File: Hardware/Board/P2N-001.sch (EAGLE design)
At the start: 40 parts, among them IC1 4053N, IC2 LTC485N, IC3 74LS07N, IC4 LTC485N, K1 G5V1, T1 2SC1815, X1 HIROSE-DX10LM1-14SE

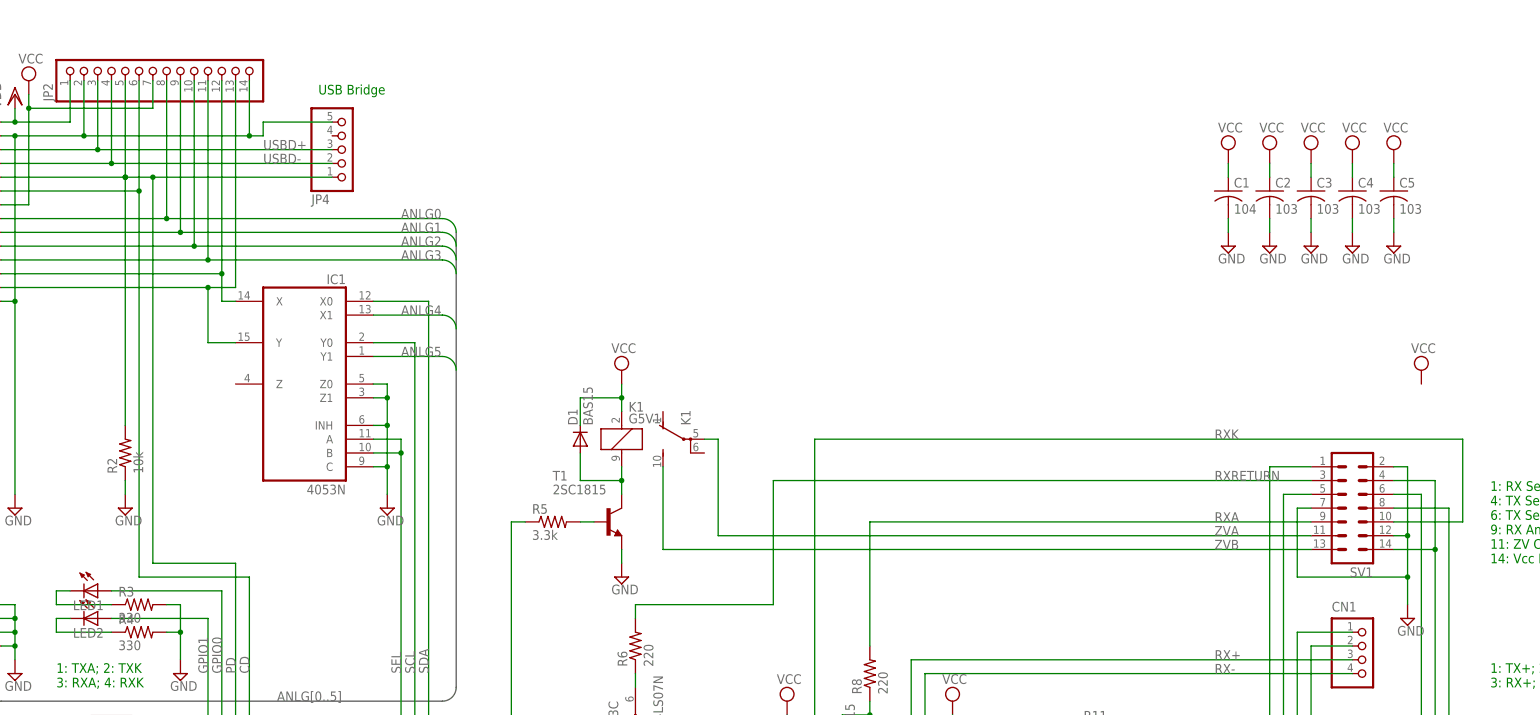
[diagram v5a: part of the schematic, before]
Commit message: Changed USB connector from Pinheader to Micro-B.
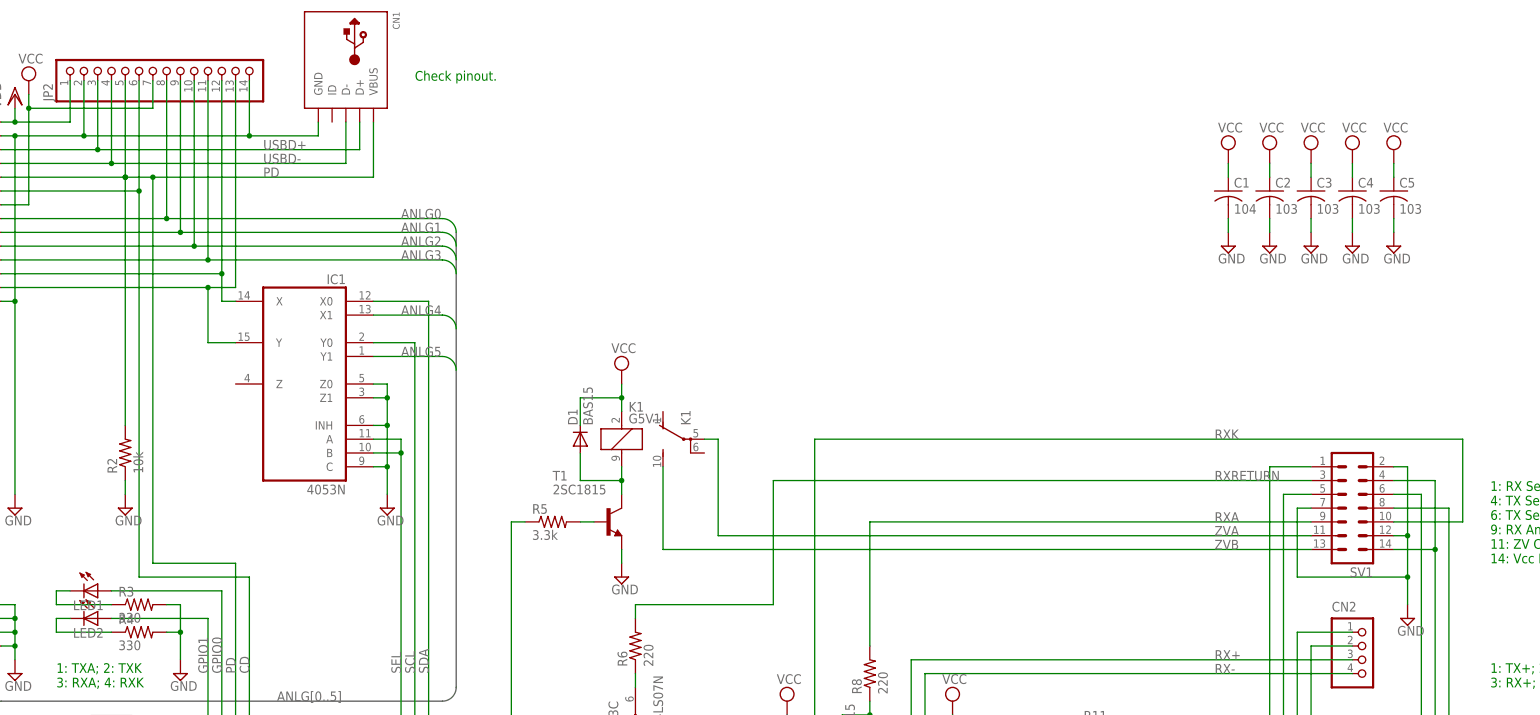
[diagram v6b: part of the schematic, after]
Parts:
- removed JP4: (no value), pinhead:PINHD-1X5/90
- added CN2: (no value), jst-ph:S4B-PH-K-S
- CN1: device jst-ph:S4B-PH-K-S -> adafruit:USBMINIB
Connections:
- net GND: now also CN1.GND; no longer JP4.5
- net PD: now also CN1.VBUS; no longer JP4.1
- net RX+: now also CN2.3; no longer CN1.3
- net RX-: now also CN2.4; no longer CN1.4
- net TX+: now also CN2.1; no longer CN1.1
- net TX-: now also CN2.2; no longer CN1.2
- net USBD+: now also CN1.D+; no longer JP4.3
- net USBD-: now also CN1.D-; no longer JP4.2
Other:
- note added: "Check pinout."
- note removed: "USB Bridge"
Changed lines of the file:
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@@
 <part name="SUPPLY26" library="supply2" deviceset="GND" device=""/>
 <part name="SUPPLY25" library="supply2" deviceset="VCC" device=""/>
-<part name="SUPPLY29" library="supply2" deviceset="GND" device=""/>
+<part name="SUPPLY28" library="supply2" deviceset="GND" device=""/>
 <part name="SUPPLY1" library="supply2" deviceset="VCC" device=""/>
 <part name="SUPPLY4" library="supply2" deviceset="VCC" device=""/>
@@
 <part name="R1" library="resistor" deviceset="R-US_" device="0204/5" value="150"/>
 <part name="SV1" library="con-ml" deviceset="ML14L" device=""/>
-<part name="JP4" library="pinhead" deviceset="PINHD-1X5" device="/90"/>
 <part name="R2" library="resistor" deviceset="R-US_" device="0204/5" value="10k"/>
 <part name="SUPPLY5" library="supply2" deviceset="GND" device=""/>
@@
 <part name="SUPPLY3" library="supply2" deviceset="GND" device=""/>
 <part name="JP1" library="pinhead" deviceset="PINHD-2X4" device=""/>
-<part name="SUPPLY28" library="supply2" deviceset="VCC" device=""/>
 <part name="K1" library="relay" deviceset="G5V1" device=""/>
-<part name="CN1" library="jst-ph" deviceset="S4B-PH-*" device="K-S"/>
+<part name="CN2" library="jst-ph" deviceset="S4B-PH-*" device="K-S"/>
 <part name="R3" library="resistor" deviceset="R-US_" device="0204/5" value="330"/>
 <part name="R4" library="resistor" deviceset="R-US_" device="0204/5" value="330"/>
@@
 <part name="R9" library="resistor" deviceset="R-US_" device="0204/5" value="220"/>
 <part name="R13" library="resistor" deviceset="R-US_" device="0204/5" value="220"/>
+<part name="CN1" library="adafruit" deviceset="USB" device="MINIB"/>
 </parts>
 <sheets>
@@
 7: LEDA; 8: LEDK</text>
 <text x="25.4" y="152.4" size="1.778" layer="91" rot="R90">GeekPort II</text>
-<text x="96.52" y="190.5" size="1.778" layer="91">USB Bridge</text>
 <text x="48.26" y="81.28" size="1.778" layer="91">1: TXA; 2: TXK
 3: RXA; 4: RXK</text>
@@
 11: ZV Contact A; 12: GND; 13: ZV Contact B;
 14: Vcc R220</text>
+<text x="114.3" y="193.04" size="1.778" layer="91">Check pinout.</text>
 </plain>
 <instances>
@@
 <instance part="IC3" gate="E" x="320.04" y="33.02"/>
 <instance part="IC3" gate="F" x="320.04" y="20.32"/>
-<instance part="SUPPLY29" gate="GND" x="307.34" y="10.16"/>
+<instance part="SUPPLY28" gate="GND" x="307.34" y="10.16"/>
 <instance part="SUPPLY1" gate="G$1" x="7.62" y="48.26"/>
 <instance part="SUPPLY4" gate="G$1" x="43.18" y="193.04"/>
@@
 <instance part="R1" gate="G$1" x="33.02" y="88.9"/>
 <instance part="SV1" gate="1" x="287.02" y="114.3" rot="R180"/>
-<instance part="JP4" gate="A" x="101.6" y="180.34" rot="MR180"/>
 <instance part="R2" gate="G$1" x="60.96" y="124.46" rot="R90"/>
 <instance part="SUPPLY5" gate="GND" x="60.96" y="114.3"/>
@@
 <instance part="SUPPLY3" gate="GND" x="40.64" y="83.82"/>
 <instance part="JP1" gate="A" x="17.78" y="91.44"/>
-<instance part="SUPPLY28" gate="G$1" x="299.72" y="139.7"/>
 <instance part="K1" gate="1" x="152.4" y="127"/>
 <instance part="K1" gate="2" x="165.1" y="127" rot="R90"/>
-<instance part="CN1" gate="G$1" x="287.02" y="88.9"/>
+<instance part="CN2" gate="G$1" x="287.02" y="88.9"/>
 <instance part="R3" gate="G$1" x="63.5" y="96.52"/>
 <instance part="R4" gate="G$1" x="63.5" y="91.44"/>
@@
 <instance part="R9" gate="G$1" x="220.98" y="68.58"/>
 <instance part="R13" gate="G$1" x="248.92" y="48.26"/>
+<instance part="CN1" gate="G$1" x="101.6" y="195.58" rot="R270"/>
 </instances>
 <busses>
@@
 </segment>
 <segment>
-<pinref part="SUPPLY29" gate="GND" pin="GND"/>
+<pinref part="SUPPLY28" gate="GND" pin="GND"/>
 <pinref part="IC3" gate="F" pin="I"/>
 <wire x1="307.34" y1="45.72" x2="307.34" y2="33.02" width="0.1524" layer="91"/>
@@
 <wire x1="40.64" y1="182.88" x2="53.34" y2="182.88" width="0.1524" layer="91"/>
 <wire x1="53.34" y1="182.88" x2="83.82" y2="182.88" width="0.1524" layer="91"/>
-<wire x1="83.82" y1="182.88" x2="86.36" y2="182.88" width="0.1524" layer="91"/>
-<wire x1="86.36" y1="182.88" x2="86.36" y2="185.42" width="0.1524" layer="91"/>
-<pinref part="JP4" gate="A" pin="5"/>
-<wire x1="86.36" y1="185.42" x2="99.06" y2="185.42" width="0.1524" layer="91"/>
 <junction x="40.64" y="182.88"/>
 <pinref part="JP2" gate="A" pin="2"/>
@@
 <pinref part="X1" gate="G$1" pin="-2"/>
 <pinref part="X1" gate="G$1" pin="-14"/>
+<pinref part="CN1" gate="G$1" pin="GND"/>
+<wire x1="83.82" y1="182.88" x2="96.52" y2="182.88" width="0.1524" layer="91"/>
+<wire x1="96.52" y1="182.88" x2="96.52" y2="185.42" width="0.1524" layer="91"/>
 </segment>
 <segment>
@@
 <wire x1="254" y1="30.48" x2="276.86" y2="30.48" width="0.1524" layer="91"/>
 <wire x1="276.86" y1="30.48" x2="276.86" y2="27.94" width="0.1524" layer="91"/>
-<pinref part="CN1" gate="G$1" pin="1"/>
+<pinref part="CN2" gate="G$1" pin="1"/>
 <wire x1="287.02" y1="91.44" x2="276.86" y2="91.44" width="0.1524" layer="91"/>
 <wire x1="276.86" y1="91.44" x2="276.86" y2="30.48" width="0.1524" layer="91"/>
@@
 <pinref part="IC2" gate="G$1" pin="A"/>
 <wire x1="175.26" y1="35.56" x2="205.74" y2="35.56" width="0.1524" layer="91"/>
-<pinref part="CN1" gate="G$1" pin="3"/>
+<pinref part="CN2" gate="G$1" pin="3"/>
 <wire x1="287.02" y1="86.36" x2="205.74" y2="86.36" width="0.1524" layer="91"/>
 <wire x1="205.74" y1="86.36" x2="205.74" y2="35.56" width="0.1524" layer="91"/>
@@
 <pinref part="IC2" gate="G$1" pin="B"/>
 <wire x1="182.88" y1="33.02" x2="180.34" y2="33.02" width="0.1524" layer="91"/>
-<pinref part="CN1" gate="G$1" pin="4"/>
+<pinref part="CN2" gate="G$1" pin="4"/>
 <wire x1="180.34" y1="33.02" x2="175.26" y2="33.02" width="0.1524" layer="91"/>
 <wire x1="287.02" y1="83.82" x2="208.28" y2="83.82" width="0.1524" layer="91"/>
@@
 <pinref part="R14" gate="G$1" pin="1"/>
 <wire x1="254" y1="27.94" x2="261.62" y2="27.94" width="0.1524" layer="91"/>
-<pinref part="CN1" gate="G$1" pin="2"/>
+<pinref part="CN2" gate="G$1" pin="2"/>
 <wire x1="261.62" y1="27.94" x2="264.16" y2="27.94" width="0.1524" layer="91"/>
 <wire x1="287.02" y1="88.9" x2="279.4" y2="88.9" width="0.1524" layer="91"/>
@@
 <net name="PD" class="0">
 <segment>
-<pinref part="JP4" gate="A" pin="1"/>
 <wire x1="38.1" y1="175.26" x2="60.96" y2="175.26" width="0.1524" layer="91"/>
 <wire x1="60.96" y1="175.26" x2="66.04" y2="175.26" width="0.1524" layer="91"/>
 <pinref part="R2" gate="G$1" pin="2"/>
 <junction x="60.96" y="175.26"/>
-<wire x1="66.04" y1="175.26" x2="99.06" y2="175.26" width="0.1524" layer="91"/>
+<wire x1="66.04" y1="175.26" x2="106.68" y2="175.26" width="0.1524" layer="91"/>
 <wire x1="60.96" y1="175.26" x2="60.96" y2="129.54" width="0.1524" layer="91"/>
 <pinref part="JP2" gate="A" pin="5"/>
@@
 <junction x="66.04" y="175.26"/>
 <pinref part="X1" gate="G$1" pin="-5"/>
+<label x="86.36" y="175.26" size="1.778" layer="95"/>
+<pinref part="CN1" gate="G$1" pin="VBUS"/>
+<wire x1="106.68" y1="185.42" x2="106.68" y2="175.26" width="0.1524" layer="91"/>
 </segment>
 </net>
 <net name="USBD-" class="0">
 <segment>
-<pinref part="JP4" gate="A" pin="2"/>
 <wire x1="38.1" y1="177.8" x2="58.42" y2="177.8" width="0.1524" layer="91"/>
 <pinref part="JP2" gate="A" pin="4"/>
-<wire x1="58.42" y1="177.8" x2="99.06" y2="177.8" width="0.1524" layer="91"/>
+<wire x1="58.42" y1="177.8" x2="101.6" y2="177.8" width="0.1524" layer="91"/>
 <wire x1="58.42" y1="193.04" x2="58.42" y2="177.8" width="0.1524" layer="91"/>
 <junction x="58.42" y="177.8"/>
 <label x="86.36" y="177.8" size="1.778" layer="95"/>
 <pinref part="X1" gate="G$1" pin="-4"/>
+<pinref part="CN1" gate="G$1" pin="D-"/>
+<wire x1="101.6" y1="185.42" x2="101.6" y2="177.8" width="0.1524" layer="91"/>
 </segment>
 </net>
 <net name="USBD+" class="0">
 <segment>
-<pinref part="JP4" gate="A" pin="3"/>
 <wire x1="38.1" y1="180.34" x2="55.88" y2="180.34" width="0.1524" layer="91"/>
 <pinref part="JP2" gate="A" pin="3"/>
-<wire x1="55.88" y1="180.34" x2="99.06" y2="180.34" width="0.1524" layer="91"/>
+<wire x1="55.88" y1="180.34" x2="104.14" y2="180.34" width="0.1524" layer="91"/>
 <wire x1="55.88" y1="193.04" x2="55.88" y2="180.34" width="0.1524" layer="91"/>
 <junction x="55.88" y="180.34"/>
 <label x="86.36" y="180.34" size="1.778" layer="95"/>
 <pinref part="X1" gate="G$1" pin="-3"/>
-</segment>
-</net>
+<pinref part="CN1" gate="G$1" pin="D+"/>
+<wire x1="104.14" y1="185.42" x2="104.14" y2="180.34" width="0.1524" layer="91"/>
+</segment>
+</net>

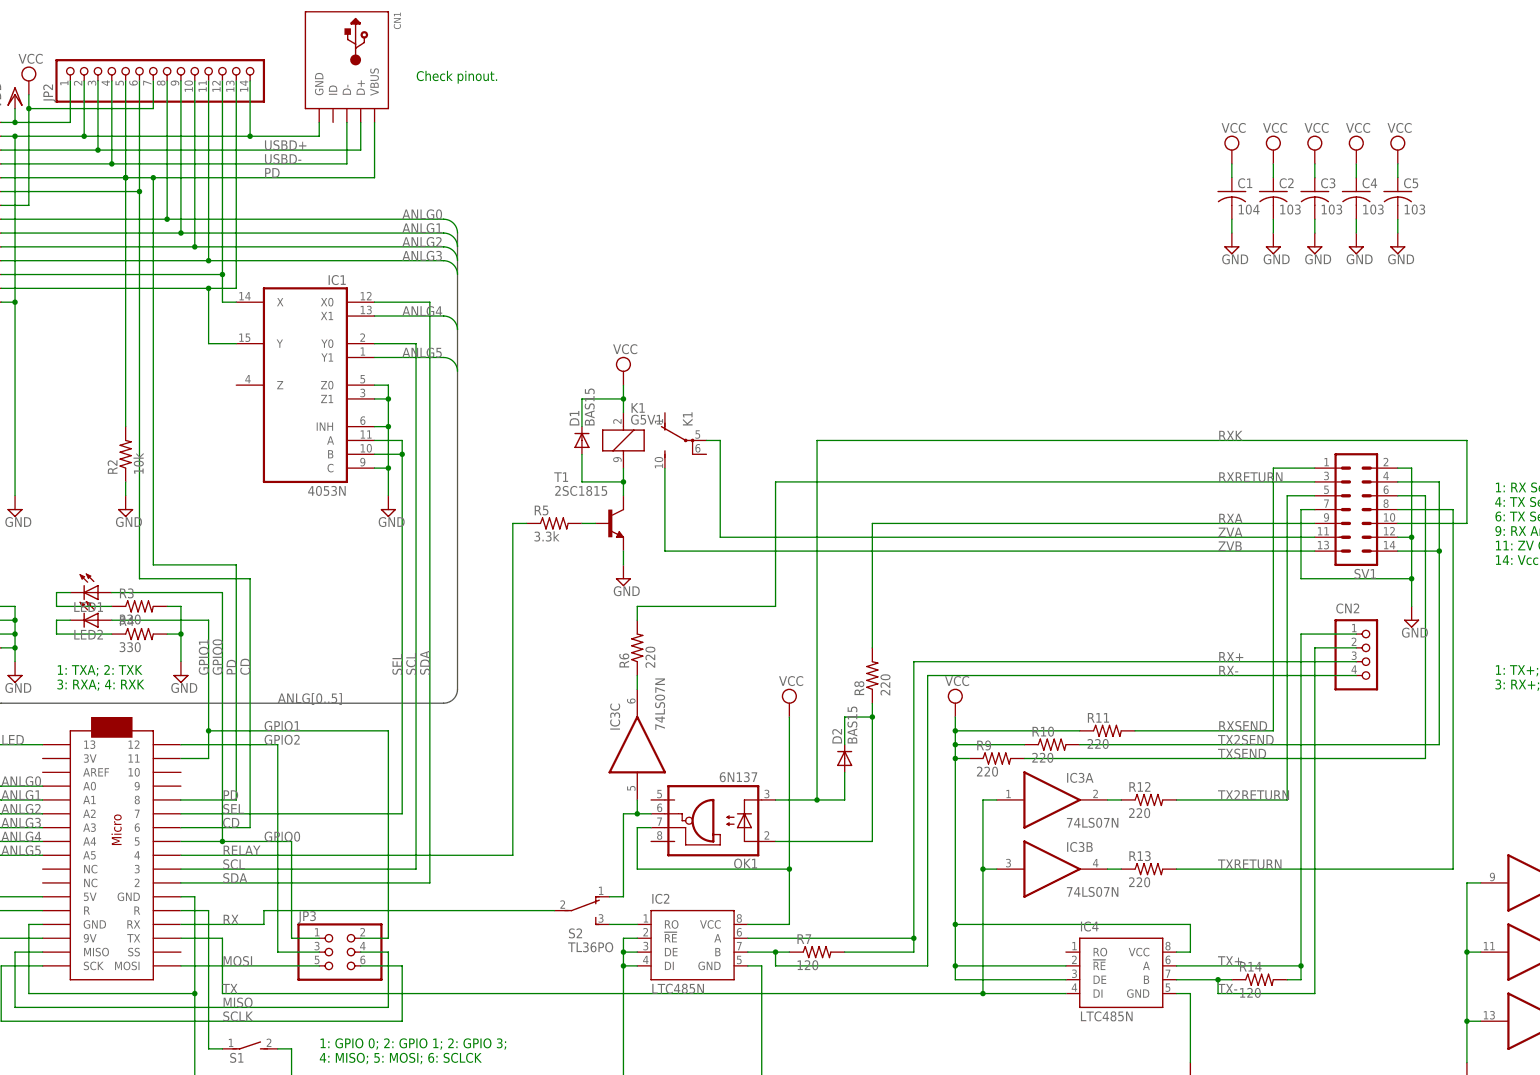
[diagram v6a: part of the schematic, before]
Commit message: Changed USB con to Sunhayatos connector board. Changed USB connector to Sunhayato's connector board. Also removed ZeroVoltage function.
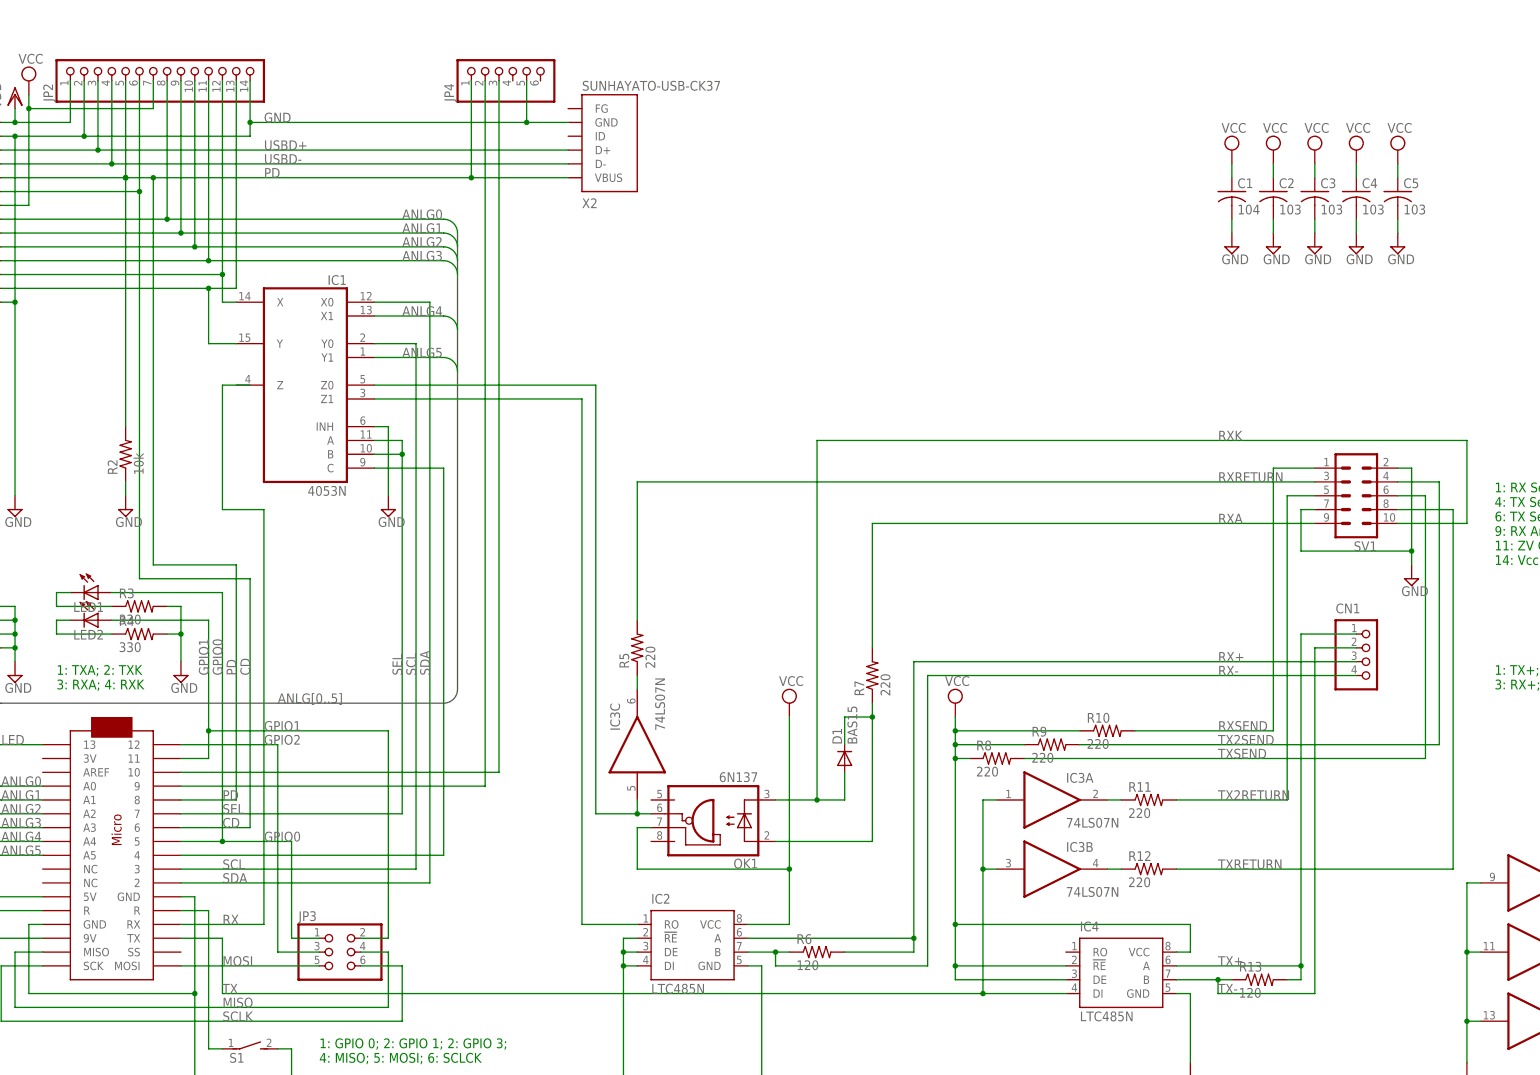
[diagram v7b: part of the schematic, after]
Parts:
- removed CN2: (no value), jst-ph:S4B-PH-K-S
- removed D2: BAS15, diode:BAS15
- removed K1: G5V1, relay:G5V1
- removed R14: 120, resistor:R-US_0204/5
- removed S2: TL36PO, switch:TL36PO
- removed T1: 2SC1815, transistor:2SC1815
- added JP4: (no value), adafruit:PINHD-1X6
- added X2: SUNHAYATO-USB-CK37, con-sunhayato-usb:SUNHAYATO-USB-CK37
- CN1: device adafruit:USBMINIB -> jst-ph:S4B-PH-K-S
- JP2: device pinhead:PINHD-1X14 -> adafruit:PINHD-1X14-CB
- R13, R6: value 220 -> 120
- R5: value 3.3k -> 220
- R7: value 120 -> 220
- SV1: device con-ml:ML14L -> con-ml:ML10L
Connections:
- removed net RELAY: MC1.4, R5.1
- removed net ZVA: K12.P, SV1.11
- removed net ZVB: K12.S, SV1.13
- new net N$5: JP4.2, MC1.9
- net GND: now also JP4.5, X2.GND; no longer CN1.GND, IC1A.C, IC1A.Z0, IC1A.Z1, SV1.12, T1.E
- net MIDIRX: now also IC1A.Z0; no longer S2.O
- net N$15: now also D1.C, R7.1; no longer D2.C, R8.1
- net N$2: now also R11.1; no longer R12.1
- net N$3: now also R5.1; no longer R6.1
- net N$4: now also R12.1; no longer R13.1
- net N$6: now also JP4.3, MC1.10; no longer D1.A, K11.2, T1.C
- net N$8: now also IC1A.C, MC1.4; no longer R5.2, T1.B
- net PD: now also JP4.1, X2.VBUS; no longer CN1.VBUS
- net RX: no longer S2.P
- net RX+: now also CN1.3, R6.2; no longer CN2.3, R7.2
- net RX-: now also CN1.4, R6.1; no longer CN2.4, R7.1
- net RXA: now also R7.2; no longer R8.2
- net RXK: now also D1.A; no longer D2.A
- net RXRETURN: now also R5.2; no longer R6.2
- net RXSEND: now also R10.2; no longer R11.2
- net TX+: now also CN1.1, R13.2; no longer CN2.1, R14.2
- net TX-: now also CN1.2, R13.1; no longer CN2.2, R14.1
- net TX2RETURN: now also R11.2; no longer R12.2
- net TX2SEND: now also R9.2; no longer R10.2, SV1.14
- net TXRETURN: now also R12.2; no longer R13.2
- net TXSEND: now also R8.2; no longer R9.2
- net USBD+: now also X2.D+; no longer CN1.D+
- net USBD-: now also X2.D-; no longer CN1.D-
- net VCC: now also R8.1; no longer D1.C, K11.1, R11.1
- net XMIDIRX: now also IC1A.Z1; no longer S2.S
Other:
- note removed: "Check pinout."
- moved on the sheet: D1, R10, R11, R12, R13, R5, R6, R7, R8, R9
